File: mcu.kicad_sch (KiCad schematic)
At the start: 17 parts, among them IC2 TCAN332, J1 Conn_01x03_Socket, J2 CAN_TERM, J3 CAN_BUS, M1 ESP32-S3-WROOM-1, U1 Varistor

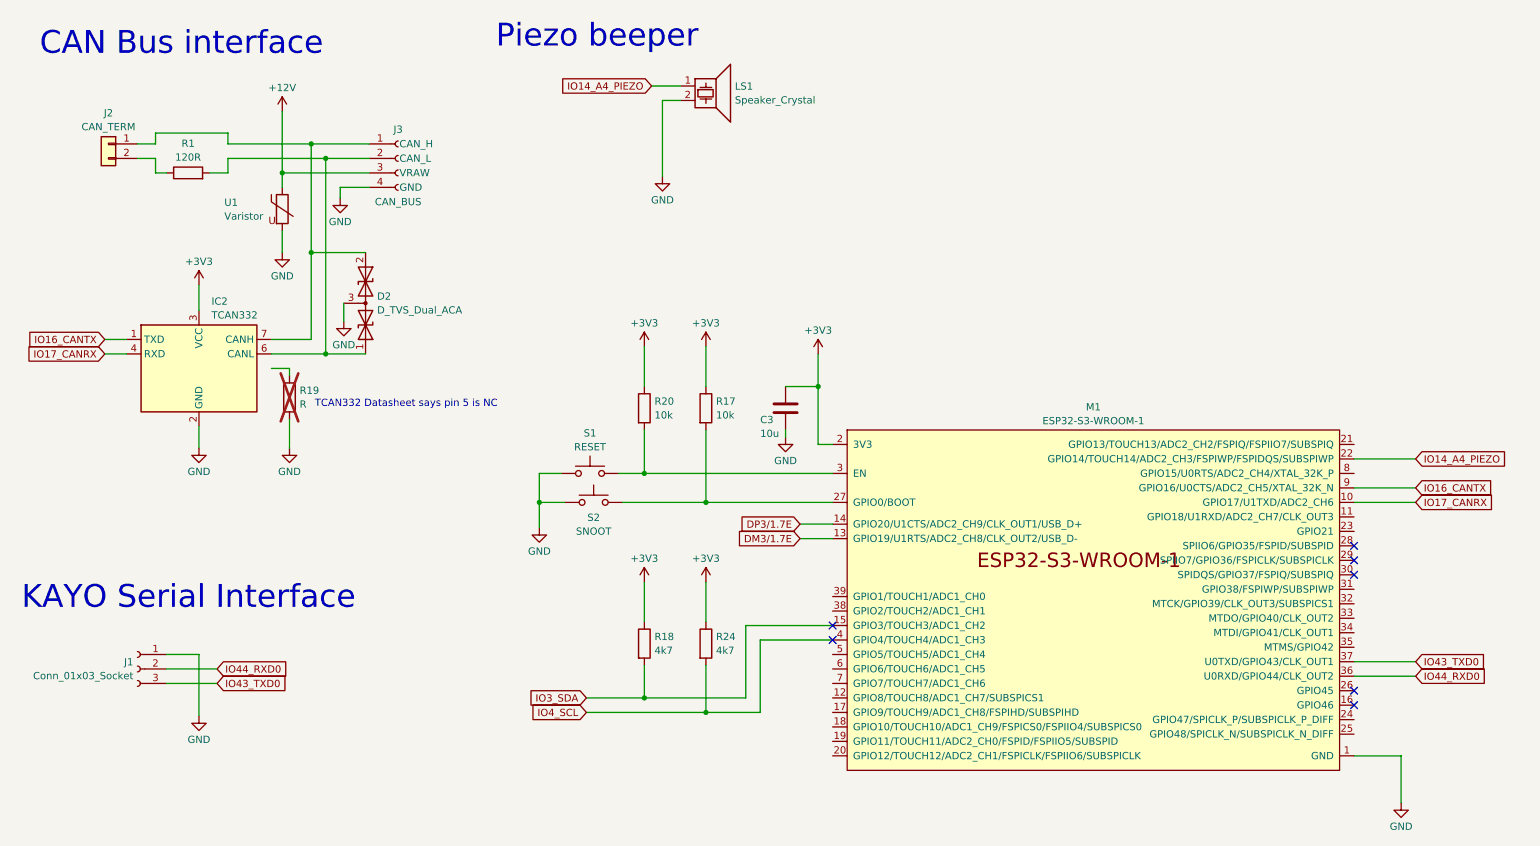
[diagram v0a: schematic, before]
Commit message: Added footprint for ESP32-S3-WROOM-1.  Aligned in schematic.
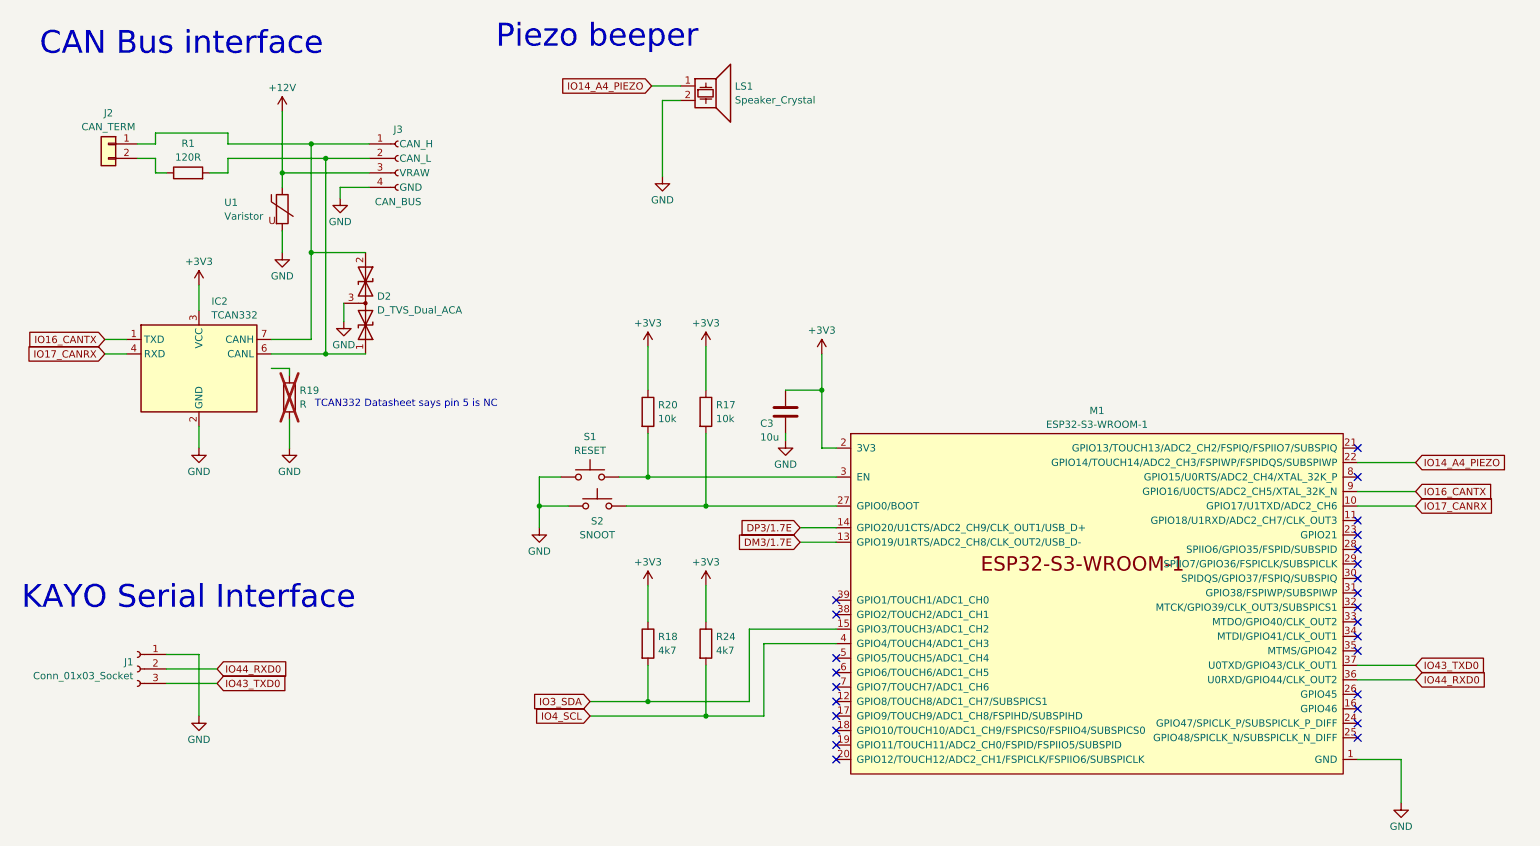
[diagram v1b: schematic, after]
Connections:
- no-connect marks 7 -> 26
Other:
- moved on the sheet: C3, M1, R17, R18, R20, S1, S2
